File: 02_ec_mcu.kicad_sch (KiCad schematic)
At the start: 46 parts, among them J16 Case power/reset button harne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, J4 TC2030 Cortex SWD: VTref/SWDI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, SW1 Reset, U4 STM32F407VGTx, U44 TCA9539PWR resettable source 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, U46 SN74LVC1G08DBVR EC-reset-qual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, U5 TPS54202DDC, Y1 J32SMX-K-F-G-I-8M0 8MHz CL8pF, Y2 X1A000141000612 32.768kHz CL6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

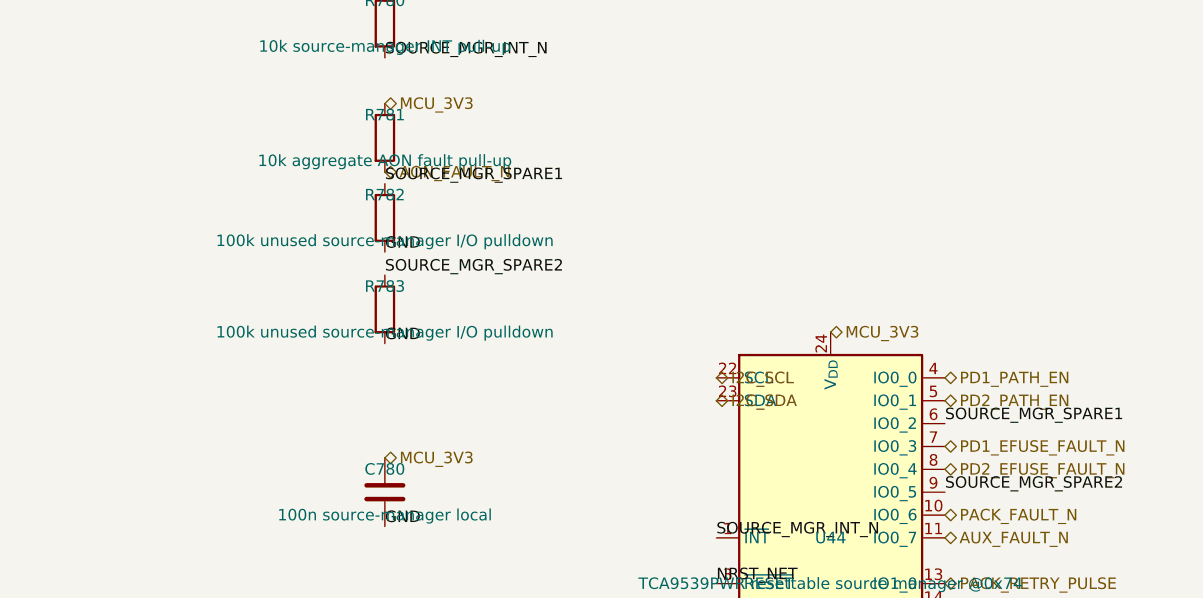
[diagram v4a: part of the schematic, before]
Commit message: Add rear 3.5mm headphone jack with plug-detect speaker mute (sheet 15)
Add the missing headphone output the user-verified behavior requires (row 11): rear CUI SJ1-3535NG stereo jack driven by a TPA6130A2RTJR DirectPath headphone amp, with automatic plug-detect speaker muting like a normal laptop.

- U425 TPA6130A2 (I2C @0x60, fixed): single-ended inputs from PCM2900C DAC_VOUT_L/R via 0.47u coupling (INM signal, INP AC-grounded per datasheet 9.2.2.1); capless ground-referenced HPLEFT/HPRIGHT outputs to jack T/R. Charge-pump flying + CPVSS + VDD bypass per 9.2.2.2/3.
- J422 SJ1-3535NG: RN ring normalling switch is plug detect (unplugged shorts RN to R = amp 0V -> low; plugged floats -> high).
- HP_DETECT is read by the EC on U44 (TCA9539 source manager) recovered spare input pin 6 (SOURCE_MGR_SPARE1 repurposed) with R782 100k pull-up to MCU_3V3. On plug-in the EC drives AUDIO_AMP_EC_EN low (U421 AND gate mutes the TPA2012D2 speaker amp) and I2C-unmutes U425.
- /SD tied to MU_HOST_ACTIVE so U425 is in hardware shutdown (0.4uA) outside S0; power-on default is muted with outputs disabled (fail-safe OFF until EC firmware enables over I2C).
- Datasheet-verified: TPA6130A2 is I2C-controlled (no G0/G1 hardware gain); reuses the TPA2012D2 WQFN-20-1EP 4x4mm EP2.7x2.7 footprint; AudioJack3_SwitchTR symbol matches the SJ1-3535NG 5-pad footprint (T/R/S/TN/RN).
- Contracts (verify_design_contracts, generate_pin_review_table x2, verify_schematic_closure) updated SPARE1->HP_DETECT. Added TPA6130A2 to sym-lib-table+LIBMAP.
- Enlarged System Audio root sheet block 60->85mm so all 14 hier pins fit; KiCad clamps sheet pins that overflow the block to the rectangle edge and merges them, which otherwise collapses I2C_SCL/HP_DETECT/AUDIO_MIC_EN into one net.
- ERC 0 errors/27 intentional warnings; schematic closure 1580/0; pin review 2603/2603.
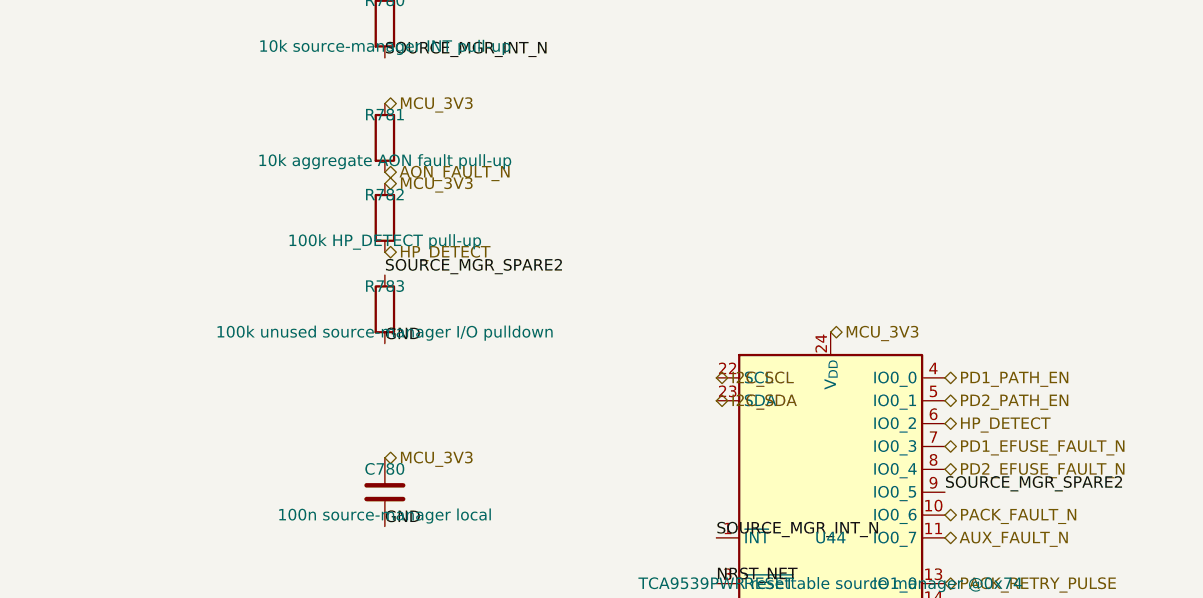
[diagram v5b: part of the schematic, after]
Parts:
- R782: value 100k unused source-manager I/O pulldown -> 100k HP_DETECT pull-up; MPN (none) -> RC0603FR-07100KL; Manufacturer (none) -> Yageo
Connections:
- net GND: no longer R782.2
- net MCU_3V3: now also R782.1
- net SOURCE_MGR_SPARE1 renamed HP_DETECT
- net HP_DETECT: now also R782.2; no longer R782.1
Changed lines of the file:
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@@
   (effects (font (size 1.27 1.27)) (justify left bottom))
 )
-(label "SOURCE_MGR_SPARE1"
+(hierarchical_label "HP_DETECT"
+  (shape bidirectional)
   (at 712.47 314.96 0)
   (effects (font (size 1.27 1.27)) (justify left bottom))
@@
   (dnp no)
   (property "Reference" "R782" (at 650.24 289.56 0) (effects (font (size 1.27 1.27))))
-  (property "Value" "100k unused source-manager I/O pulldown" (at 650.24 294.64 0) (effects (font (size 1.27 1.27))))
+  (property "Value" "100k HP_DETECT pull-up" (at 650.24 294.64 0) (effects (font (size 1.27 1.27))))
   (property "Footprint" "Resistor_SMD:R_0603_1608Metric" (at 650.24 292.1 0) (effects (font (size 1.27 1.27)) (hide yes)))
   (property "Datasheet" "" (at 650.24 292.1 0) (effects (font (size 1.27 1.27)) (hide yes)))
+  (property "Manufacturer" "Yageo" (at 650.24 292.1 0) (effects (font (size 1.27 1.27)) (hide yes)))
+  (property "MPN" "RC0603FR-07100KL" (at 650.24 292.1 0) (effects (font (size 1.27 1.27)) (hide yes)))
   (pin "1")
   (pin "2")
@@
   )
 )
-(label "SOURCE_MGR_SPARE1"
+(hierarchical_label "MCU_3V3"
+  (shape bidirectional)
   (at 650.24 288.29 0)
   (effects (font (size 1.27 1.27)) (justify left bottom))
 )
-(label "GND"
+(hierarchical_label "HP_DETECT"
+  (shape bidirectional)
   (at 650.24 295.91 0)
   (effects (font (size 1.27 1.27)) (justify left bottom))

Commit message: Stamp generation-time BOM catalog; close 378 procurement gaps
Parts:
- C20, C21, C22, C23, C24, C25, C27, C31, C38, C780, C781: MPN (none) -> GRM188R71H104KA93D; Manufacturer (none) -> Murata
- C26: MPN (none) -> GRM21BR71A475KA73L; Manufacturer (none) -> Murata
- C28: MPN (none) -> GRM21BR71A105KA01L; Manufacturer (none) -> Murata
- C29, C30: MPN (none) -> GRM21BR60J225ME01; Manufacturer (none) -> Murata
- C290: MPN (none) -> GRM188R71H103KA01; Manufacturer (none) -> Murata
- C292: MPN (none) -> GRM1555C1H560JA01; Manufacturer (none) -> Murata
- R32, R33, R780, R781: MPN (none) -> RC0603FR-0710KL; Manufacturer (none) -> Yageo
- R34, R37: MPN (none) -> RC0603FR-070RL; Manufacturer (none) -> Yageo
- R35, R783: MPN (none) -> RC0603FR-07100KL; Manufacturer (none) -> Yageo
- R36: MPN (none) -> RC0603FR-0722K1L; Manufacturer (none) -> Yageo

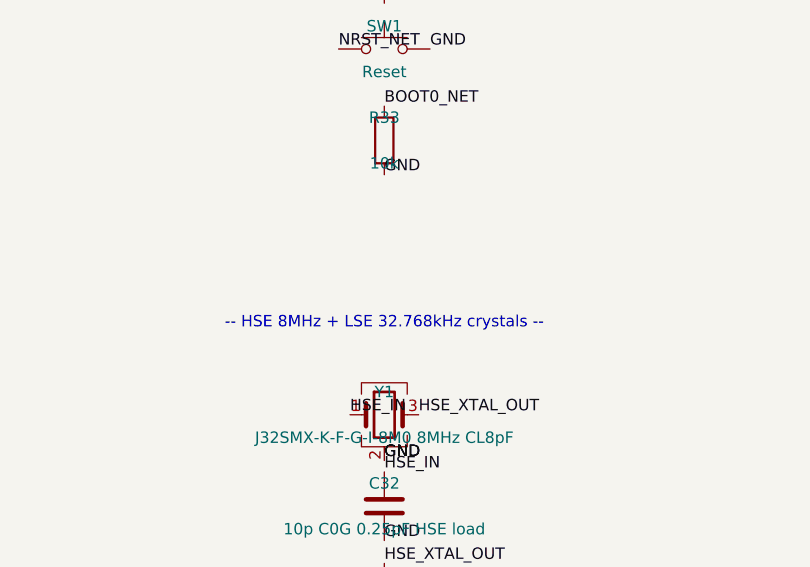
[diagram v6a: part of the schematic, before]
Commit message: Complete EC DFU port (J73) + DB power rework; verify schematic and board
- Add rear USB-C EC firmware programming port J73 (UFP/DFU) on Internal
  Services sheet: USBLC6-2P6 ESD (U63), 5.1k CC Rd resistors (R205/R211),
  22R series on D+/D- (R203/R204), mux-select hookup so BOOT0 high forces
  the USB mux to the DFU port
- Rename port ref J70->J73 after ham-radio collision; sync all net names
  (J73_CC1/J73_CC2)
- DB power rework: S5 gating + 3V3_STBY split, dual DCDC paths, GND
  returns on the standby rails; regenerate all sheets and re-verify
- sync_main_pcb_from_netlist: anchor placement for the 9 new footprints,
  scoped ECO support
- Board: rebuild main PCB with J73 footprint block (lib-sourced, net
  injection from netlist name attribute), sync pad nets for the 5 stale
  refs, remove duplicate R205/R211 copies
- Verified: check_schematic self-check OK (0 errors), radio DB contracts
  OK, ERC 0 errors, board DRC 0 electrical violations, board-vs-schematic
  net parity 0 conflicts, no duplicate refs
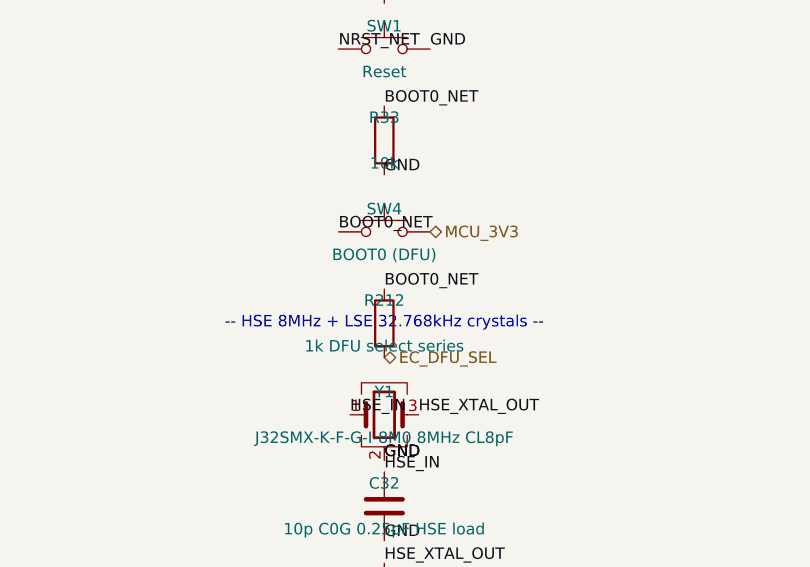
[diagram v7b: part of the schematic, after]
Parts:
- removed C32, C33: 10p C0G 0.25pF HSE load, Capacitor_SMD:C_0603_1608Metric, symbol Device:C
- removed C36: 10u 50V X7R VIN, Capacitor_SMD:C_1206_3216Metric, symbol Device:C
- removed C37: 100n 50V X7R VIN HF, Capacitor_SMD:C_0603_1608Metric, symbol Device:C
- removed R780: 10k source-manager INT pull-up, Resistor_SMD:R_0603_1608Metric, symbol Device:R
- removed R781: 10k aggregate AON fault pull-up, Resistor_SMD:R_0603_1608Metric, symbol Device:R
- added C291: 22u 16V X7R MCU_3V3 output, Capacitor_SMD:C_1206_3216Metric, symbol Device:C
- added C292: 56p C0G TPS54202 feed-forward, Capacitor_SMD:C_0402_1005Metric, symbol Device:C
- added C34, C35: 6.8p C0G 0.25pF LSE load, Capacitor_SMD:C_0603_1608Metric, symbol Device:C
- added R172: 100k service mux reset-request pull-up, Resistor_SMD:R_0603_1608Metric, symbol Device:R
- added R212: 1k DFU select series, Resistor_SMD:R_0603_1608Metric, symbol Device:R
- added SW4: BOOT0 (DFU), Button_Switch_SMD:SW_SPST_B3S-1000, symbol Switch:SW_Push
- added U46: SN74LVC1G08DBVR EC-reset-qualified service mux re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, Package_TO_SOT_SMD:SOT-23-5, symbol 74xGxx:74LVC1G08
- C32: renamed from R37; value 0R HSE drive/tuning position -> 10p C0G 0.25pF HSE load; footprint Resistor_SMD:R_0603_1608Metric -> Capacitor_SMD:C_0603_1608Metric; symbol Device:R -> Device:C; MPN RC0603FR-070RL -> C0603C100C5GACTU; Manufacturer Yageo -> KEMET
- C33: renamed from Y2; value X1A000141000612 32.768kHz CL6pF -> 10p C0G 0.25pF HSE load; footprint Crystal:Crystal_SMD_3215-2Pin_3.2x1.5mm -> Capacitor_SMD:C_0603_1608Metric; symbol Device:Crystal -> Device:C; MPN X1A000141000612 -> C0603C100C5GACTU; Manufacturer Epson -> KEMET
- C36: renamed from C38; value 100n (BOOT cap) -> 10u 50V X7R VIN; footprint Capacitor_SMD:C_0603_1608Metric -> Capacitor_SMD:C_1206_3216Metric; MPN GRM188R71H104KA93D -> CGA5L1X7R1H106K160AC; Manufacturer Murata -> TDK
- C37: renamed from L3; value 10uH 20% 3.3A Isat20 -> 100n 50V X7R VIN HF; footprint ducktop2:Coilcraft_XGL5030 -> Capacitor_SMD:C_0603_1608Metric; symbol Device:L -> Device:C; MPN XGL5030-103MEC -> GRM188R71H104KA93D; Manufacturer Coilcraft -> Murata
- C38: renamed from R35; value 100k 1% (3.3V FB hi) -> 100n (BOOT cap); footprint Resistor_SMD:R_0603_1608Metric -> Capacitor_SMD:C_0603_1608Metric; symbol Device:R -> Device:C; MPN RC0603FR-07100KL -> GRM188R71H104KA93D; Manufacturer Yageo -> Murata
- C39: renamed from C292; value 56p C0G TPS54202 feed-forward -> 22u 16V X7R MCU_3V3 output; footprint Capacitor_SMD:C_0402_1005Metric -> Capacitor_SMD:C_1206_3216Metric; MPN GRM1555C1H560JA01 -> GRM31CZ71C226ME15L
- C780: renamed from U46; value SN74LVC1G08DBVR EC-reset-qualified service mux reset -> 100n source-manager local; footprint Package_TO_SOT_SMD:SOT-23-5 -> Capacitor_SMD:C_0603_1608Metric; symbol 74xGxx:74LVC1G08 -> Device:C; MPN SN74LVC1G08DBVR -> GRM188R71H104KA93D; Manufacturer Texas Instruments -> Murata; ResetContract U45 RESET_N = EC NRST AND firmware reset request -> (none)
- L3: renamed from R36; value 22.1k 1% (3.3V FB lo) -> 10uH 20% 3.3A Isat20; footprint Resistor_SMD:R_0603_1608Metric -> ducktop2:Coilcraft_XGL5030; symbol Device:R -> Device:L; MPN RC0603FR-0722K1L -> XGL5030-103MEC; Manufacturer Yageo -> Coilcraft
- R35: renamed from C39; value 22u 16V X7R MCU_3V3 output -> 100k 1% (3.3V FB hi); footprint Capacitor_SMD:C_1206_3216Metric -> Resistor_SMD:R_0603_1608Metric; symbol Device:C -> Device:R; MPN GRM31CZ71C226ME15L -> RC0603FR-07100KL; Manufacturer Murata -> Yageo
- R36: renamed from C291; value 22u 16V X7R MCU_3V3 output -> 22.1k 1% (3.3V FB lo); footprint Capacitor_SMD:C_1206_3216Metric -> Resistor_SMD:R_0603_1608Metric; symbol Device:C -> Device:R; MPN GRM31CZ71C226ME15L -> RC0603FR-0722K1L; Manufacturer Murata -> Yageo
- R37: renamed from C34; value 6.8p C0G 0.25pF LSE load -> 0R HSE drive/tuning position; footprint Capacitor_SMD:C_0603_1608Metric -> Resistor_SMD:R_0603_1608Metric; symbol Device:C -> Device:R; MPN C0603C689C5GACTU -> RC0603FR-070RL; Manufacturer KEMET -> Yageo
- R780: renamed from R782; value 100k HP_DETECT pull-up -> 10k source-manager INT pull-up; MPN RC0603FR-07100KL -> RC0603FR-0710KL
- R781: renamed from R783; value 100k unused source-manager I/O pulldown -> 10k aggregate AON fault pull-up; MPN RC0603FR-07100KL -> RC0603FR-0710KL
- R782: renamed from C780; value 100n source-manager local -> 100k HP_DETECT pull-up; footprint Capacitor_SMD:C_0603_1608Metric -> Resistor_SMD:R_0603_1608Metric; symbol Device:C -> Device:R; MPN GRM188R71H104KA93D -> RC0603FR-07100KL; Manufacturer Murata -> Yageo
- R783: renamed from R172; value 100k service mux reset-request pull-up -> 100k unused source-manager I/O pulldown
- Y2: renamed from C35; value 6.8p C0G 0.25pF LSE load -> X1A000141000612 32.768kHz CL6pF; footprint Capacitor_SMD:C_0603_1608Metric -> Crystal:Crystal_SMD_3215-2Pin_3.2x1.5mm; symbol Device:C -> Device:Crystal; MPN C0603C689C5GACTU -> X1A000141000612; Manufacturer KEMET -> Epson
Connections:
- net AON_FAULT_N: now also R781.2
- net BOOT0_NET: now also R212.1, SW4.1
- net BUCK_BOOT: now also C38.1; no longer C36.1
- net BUCK_FB: now also R35.2, R36.1, C292.2; no longer C38.2, C39.2, L3.1
- net BUCK_SW: now also C38.2, L3.1; no longer C36.2, C37.1
- net EC_AON_IN: now also C36.1, C37.1
- net GND: now also C32.2, C33.2, C36.2, C37.2, C39.2, C780.2, R783.2, C291.2, C34.2, C35.2, U46.3 (GND); no longer C780.3 (GND), L3.2, R35.2, R37.2, R781.2, R782.2, Y2.2
- net HP_DETECT: now also R782.2; no longer R780.2
- net HSE_IN: now also C32.1
- net HSE_OUT: now also R37.2; no longer C32.2
- net HSE_XTAL_OUT: now also C33.1, R37.1; no longer C32.1
- net LSE_IN: now also Y2.1, C34.1; no longer C33.1, R37.1
- net LSE_OUT: now also Y2.2, C35.1; no longer C33.2, Y2.1
- net MCU_3V3: now also C780.1, L3.2, R781.1, C291.1, C292.1, R172.1, SW4.2, U46.5 (VCC); no longer C37.2, C38.1, C780.5 (VCC), R36.1, R783.1
- net NRST_NET: now also U46.1; no longer C780.1
- net SERVICE_MUX_RESET_N: now also U46.4; no longer C780.4
- net SERVICE_MUX_RESET_REQ_N: now also R172.2, U46.2; no longer C780.2, R783.2
- net SOURCE_MGR_INT_N: now also R780.2
- net SOURCE_MGR_SPARE2: now also R783.1; no longer R781.1
- new net EC_DFU_SEL: R212.2
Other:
- moved on the sheet: C36, C39, R780, R781, R783
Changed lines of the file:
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@@
+  (effects (font (size 1.27 1.27)) (justify left bottom))
+)
+(symbol
+  (lib_id "Switch:SW_Push")
+  (at 20.32 219.71 0)
+  (unit 0)
+  (exclude_from_sim no)
+  (in_bom yes)
+  (on_board yes)
+  (dnp no)
+  (property "Reference" "SW4" (at 20.32 217.17 0) (effects (font (size 1.27 1.27))))
+  (property "Value" "BOOT0 (DFU)" (at 20.32 222.25 0) (effects (font (size 1.27 1.27))))
+  (property "Footprint" "Button_Switch_SMD:SW_SPST_B3S-1000" (at 20.32 219.71 0) (effects (font (size 1.27 1.27)) (hide yes)))
+  (property "Datasheet" "" (at 20.32 219.71 0) (effects (font (size 1.27 1.27)) (hide yes)))
+  (property "Manufacturer" "Omron" (at 20.32 219.71 0) (effects (font (size 1.27 1.27)) (hide yes)))
+  (property "MPN" "B3S-1000" (at 20.32 219.71 0) (effects (font (size 1.27 1.27)) (hide yes)))
+  (property "MechanicalRole" "Case pinhole access; hold at EC reset to enter USB DFU" (at 20.32 219.71 0) (effects (font (size 1.27 1.27)) (hide yes)))
+  (pin "1")
+  (pin "2")
+  (instances
+    (project "ducktop2"
+      (path "/ed7eaa34-1bd3-577a-ab85-6415c5cdb1f8"
+        (reference "SW4")
+        (unit 0)
+      )
+    )
+  )
+)
+(label "BOOT0_NET"
+  (at 15.24 219.71 0)
+  (effects (font (size 1.27 1.27)) (justify left bottom))
+)
+(hierarchical_label "MCU_3V3"
+  (shape bidirectional)
+  (at 25.4 219.71 0)
+  (effects (font (size 1.27 1.27)) (justify left bottom))
+)
+(symbol
+  (lib_id "Device:R")
+  (at 20.32 229.87 0)
+  (unit 1)
+  (exclude_from_sim no)
+  (in_bom yes)
+  (on_board yes)
+  (dnp no)
+  (property "Reference" "R212" (at 20.32 227.33 0) (effects (font (size 1.27 1.27))))
+  (property "Value" "1k DFU select series" (at 20.32 232.41 0) (effects (font (size 1.27 1.27))))
+  (property "Footprint" "Resistor_SMD:R_0603_1608Metric" (at 20.32 229.87 0) (effects (font (size 1.27 1.27)) (hide yes)))
+  (property "Datasheet" "" (at 20.32 229.87 0) (effects (font (size 1.27 1.27)) (hide yes)))
+  (pin "1")
+  (pin "2")
+  (instances
+    (project "ducktop2"
+      (path "/ed7eaa34-1bd3-577a-ab85-6415c5cdb1f8"
+        (reference "R212")
+        (unit 1)
+      )
+    )
+  )
+)
+(label "BOOT0_NET"
+  (at 20.32 226.06 0)
+  (effects (font (size 1.27 1.27)) (justify left bottom))
+)
+(hierarchical_label "EC_DFU_SEL"
+  (shape bidirectional)
+  (at 20.32 233.68 0)
   (effects (font (size 1.27 1.27)) (justify left bottom))
 )
